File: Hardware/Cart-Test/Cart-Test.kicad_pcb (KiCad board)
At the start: 2 copper layers, 133.6 x 35.7 mm, 2 parts, among them P1 72-Pin Connector, P2 72-Pin Connector

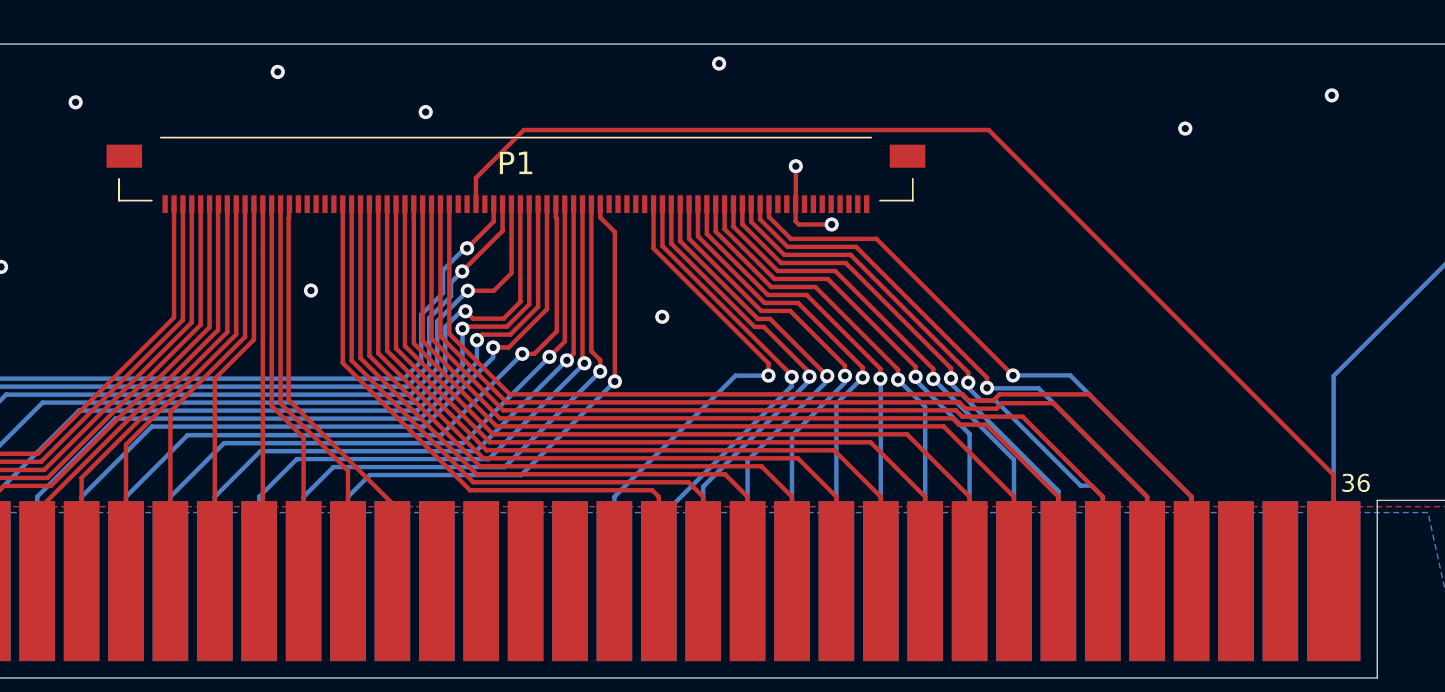
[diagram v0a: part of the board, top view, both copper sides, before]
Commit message: + Updated FFC footprint on Cart Slot and Cart-Test
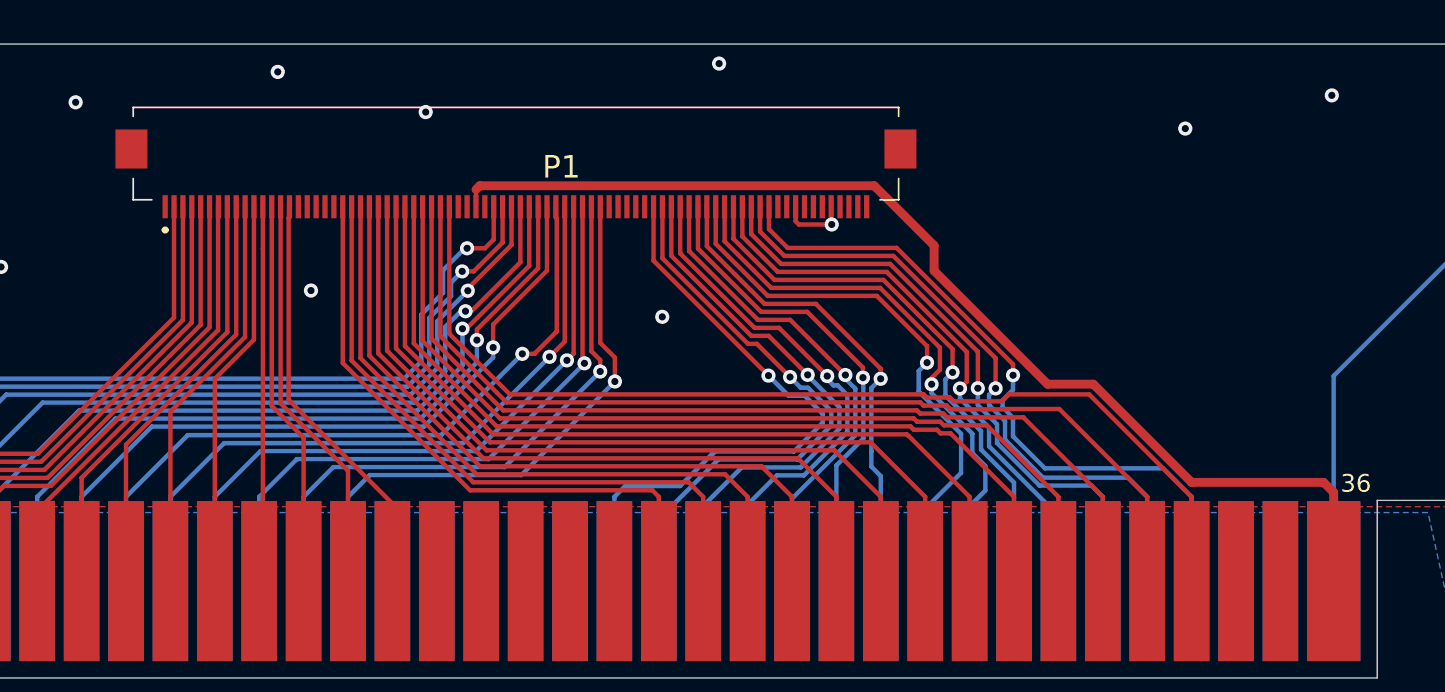
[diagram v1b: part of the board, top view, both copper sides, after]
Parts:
- P1: footprint SamacSys_Parts:5051108091 -> TinyTendo:XF3M80151BE
- moved P1 2.57 mm to (336.9, 122.3)
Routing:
- net /PPU-~WE: track 28.7 -> 35.1 mm
- net /VRAM-~CE: track 27.5 -> 32.5 mm
- net /PPU-A10: track 27.8 -> 32.0 mm
- net /PPU-~A13: track 27.3 -> 30.9 mm
- net /PPU-D4: track 35.8 -> 39.1 mm
- net /PPU-A12: track 28.9 -> 31.9 mm
- net /PPU-D5: track 34.3 -> 37.1 mm
- net /VCC: track 64.9 -> 62.2 mm
- net /PPU-A7: track 27.0 -> 29.3 mm
- net /PPU-D6: track 32.9 -> 35.2 mm
- net /GND: track 46.0 -> 43.9 mm, vias 20 -> 19
- net /PPU-A13: track 29.9 -> 31.9 mm
- net /PPU-D7: track 30.7 -> 32.5 mm
- net /CPU-A14: track 48.8 -> 47.2 mm
- net /CPU-D7: track 46.3 -> 45.0 mm
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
